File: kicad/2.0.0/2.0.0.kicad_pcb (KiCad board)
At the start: 2 copper layers, 55 parts, among them J1 DIFFX, J2 DIFFY, J3 POWER, J4 SUM, U1 OPA2197, U2 OPA2197, U3 LM317, U4 LM337, U5 OPA2197, U6 OPA197

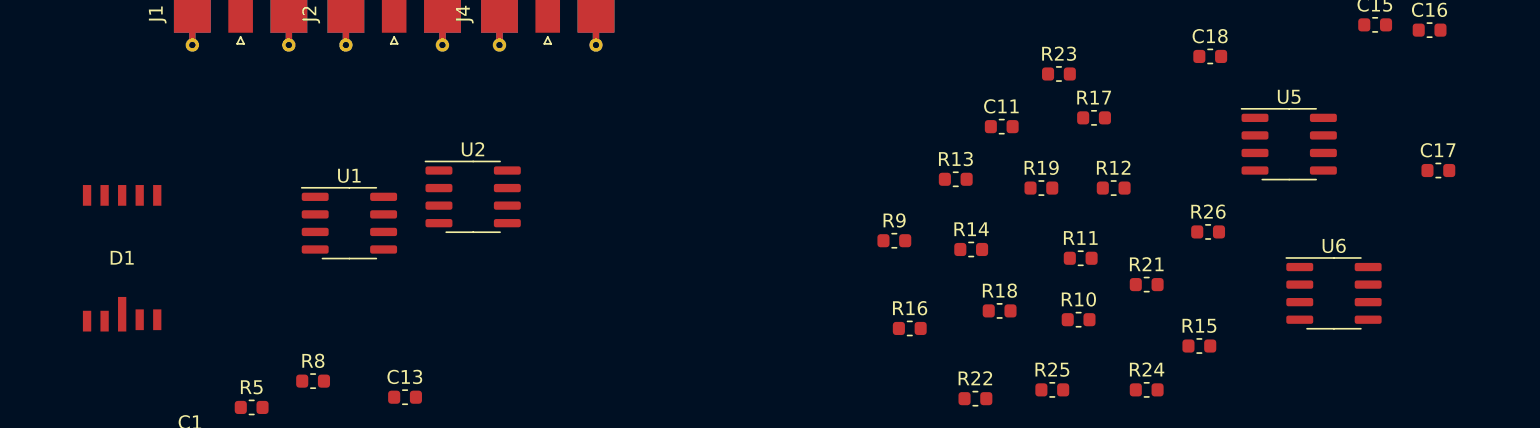
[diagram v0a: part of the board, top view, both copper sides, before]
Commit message: updated footprints of S5990, OPA197 and OPA2197
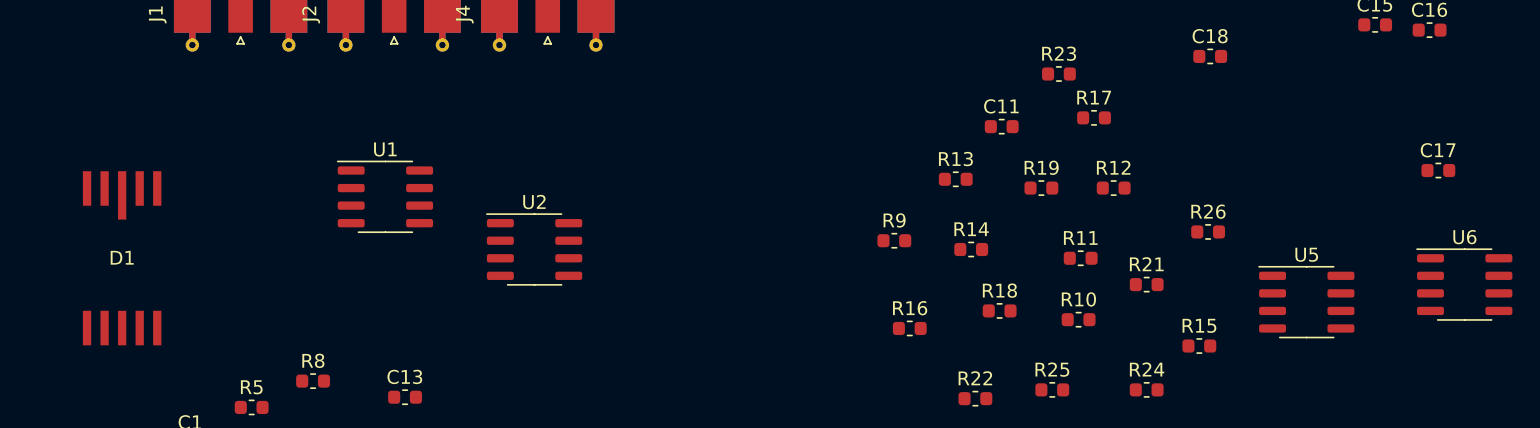
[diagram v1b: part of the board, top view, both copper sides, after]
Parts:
- U1, U2, U5: value OPA2197 -> OPA2197IDR
- U6: value OPA197 -> OPA197IDR
- moved U5 11.5 mm to (137.2, 81.3)
- moved U6 9.48 mm to (148.6, 80.0)
- moved U2 5.85 mm to (81.3, 77.5)
- moved U1 3.23 mm to (70.5, 73.7)
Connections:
- U5 pad 4: +12V -> -12V
- U5 pad 8: -12V -> +12V
- U6 pad 1: /SUM -> (no net)
- U6 pad 6: (no net) -> /SUM
- U6 pad 7: (no net) -> +12V
- U6 pad 8: +12V -> (no net)

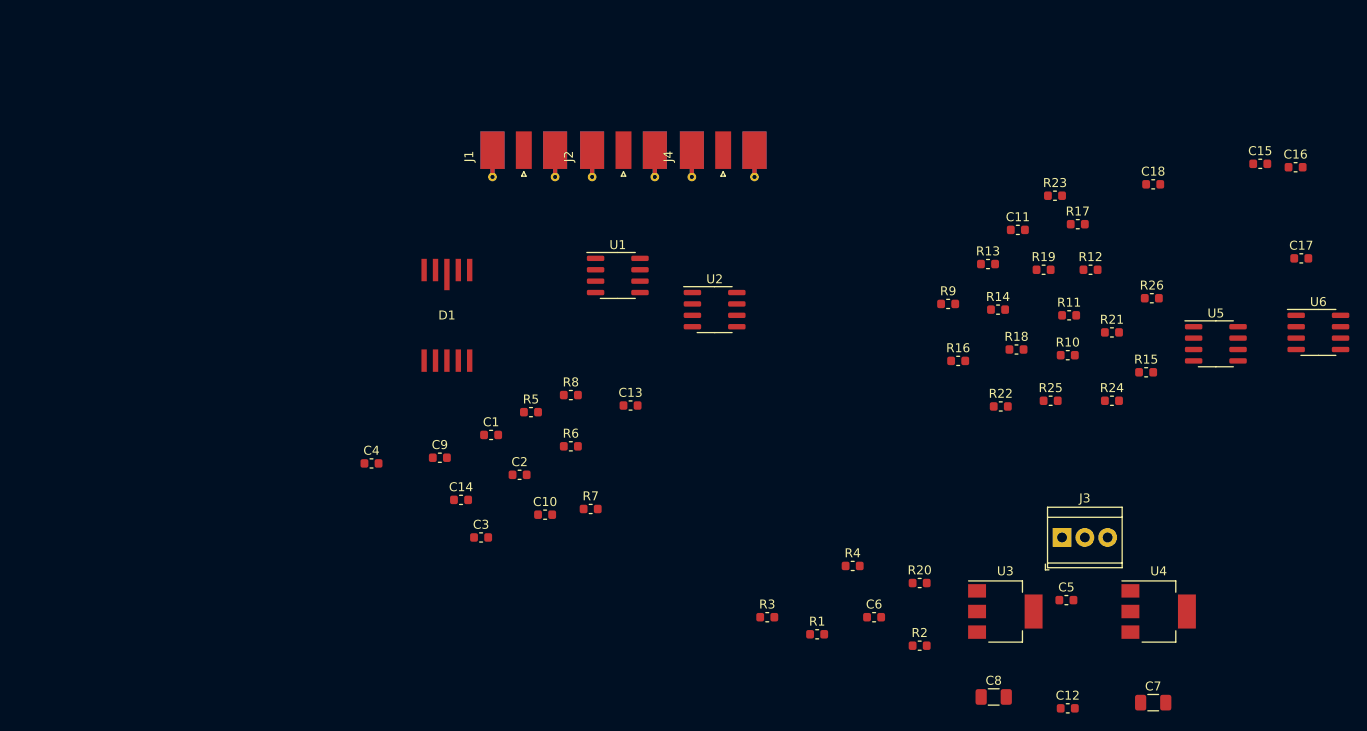
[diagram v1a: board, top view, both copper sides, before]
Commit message: updated S5990 symbol to show pin number
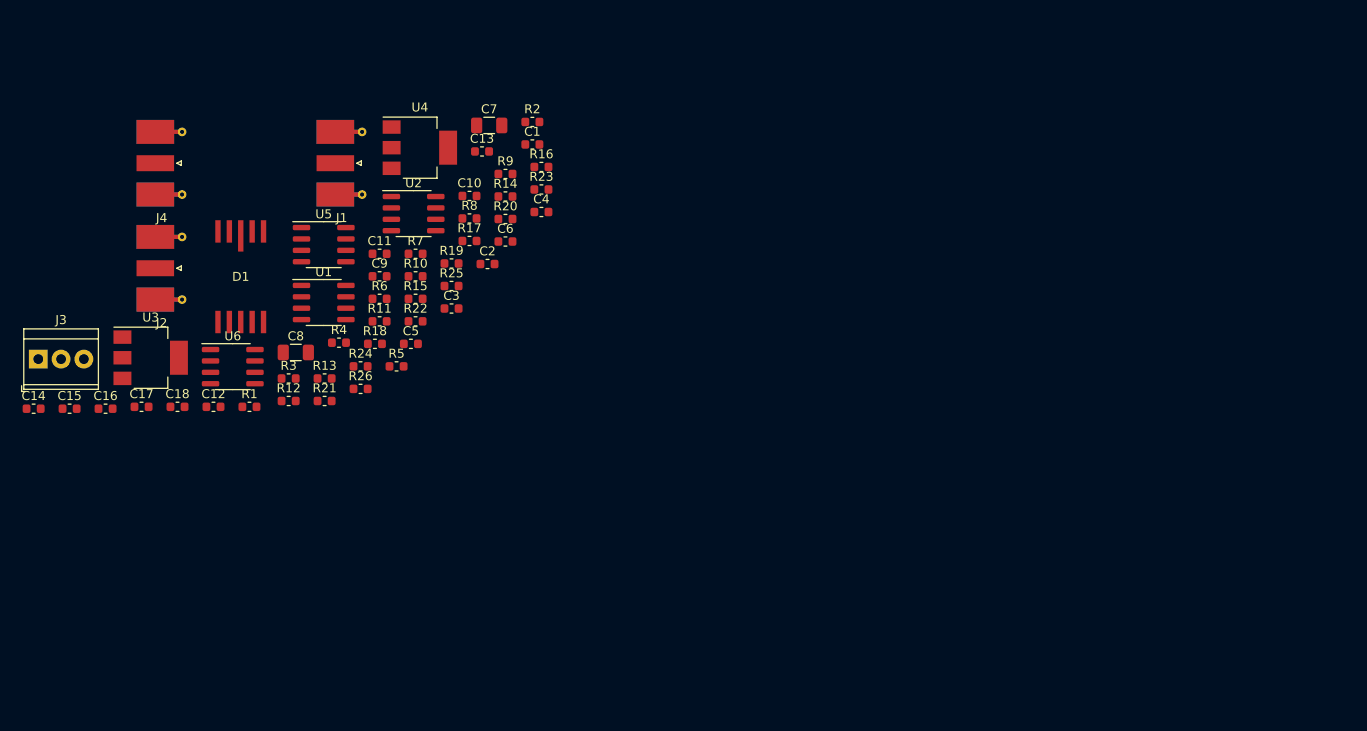
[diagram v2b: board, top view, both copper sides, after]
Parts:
- moved C15 135.5 mm to (9.37, 88.5)
- moved C16 135.4 mm to (13.4, 88.5)
- moved C17 130.3 mm to (17.4, 88.3)
- moved U6 121.1 mm to (27.6, 83.8)
- moved J3 115.9 mm to (5.88, 83.0)
- moved C18 111.6 mm to (21.4, 88.3)
- moved C12 101.0 mm to (25.4, 88.3)
- moved U5 100.1 mm to (37.7, 70.2)
- moved U3 99.4 mm to (18.4, 82.8)
- moved C7 98.1 mm to (56.1, 56.9)
- moved U4 97.3 mm to (48.4, 59.4)
- moved R12 90.6 mm to (33.8, 87.7)
- moved R26 88.8 mm to (41.8, 86.3)
- moved R21 88.1 mm to (37.8, 87.7)
- moved C8 86.8 mm to (34.6, 82.2)
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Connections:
- D1 pad 10: Net-(C10-Pad2) -> Net-(C14-Pad2)
- D1 pad 5: Net-(C14-Pad2) -> Net-(C10-Pad2)
- U6 pad 2: Net-(R21-Pad1) -> Net-(U6-Pad2)
- U6 pad 3: Net-(R25-Pad1) -> Net-(U6-Pad3)
- U6 pad 4: -12V -> Net-(U6-Pad4)
- U6 pad 6: /SUM -> Net-(U6-Pad6)
- U6 pad 7: +12V -> Net-(U6-Pad7)

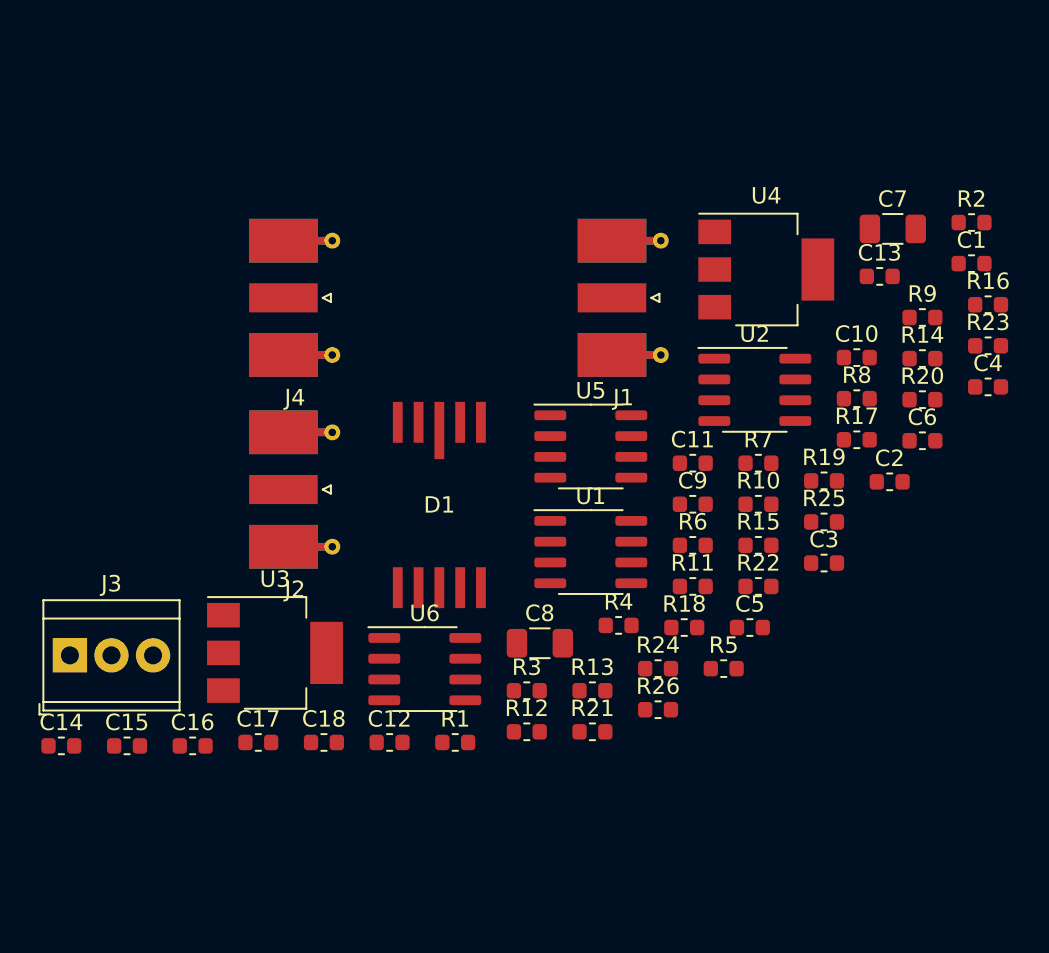
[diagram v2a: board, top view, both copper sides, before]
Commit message: grouped components for 2.0.0 design on pcb
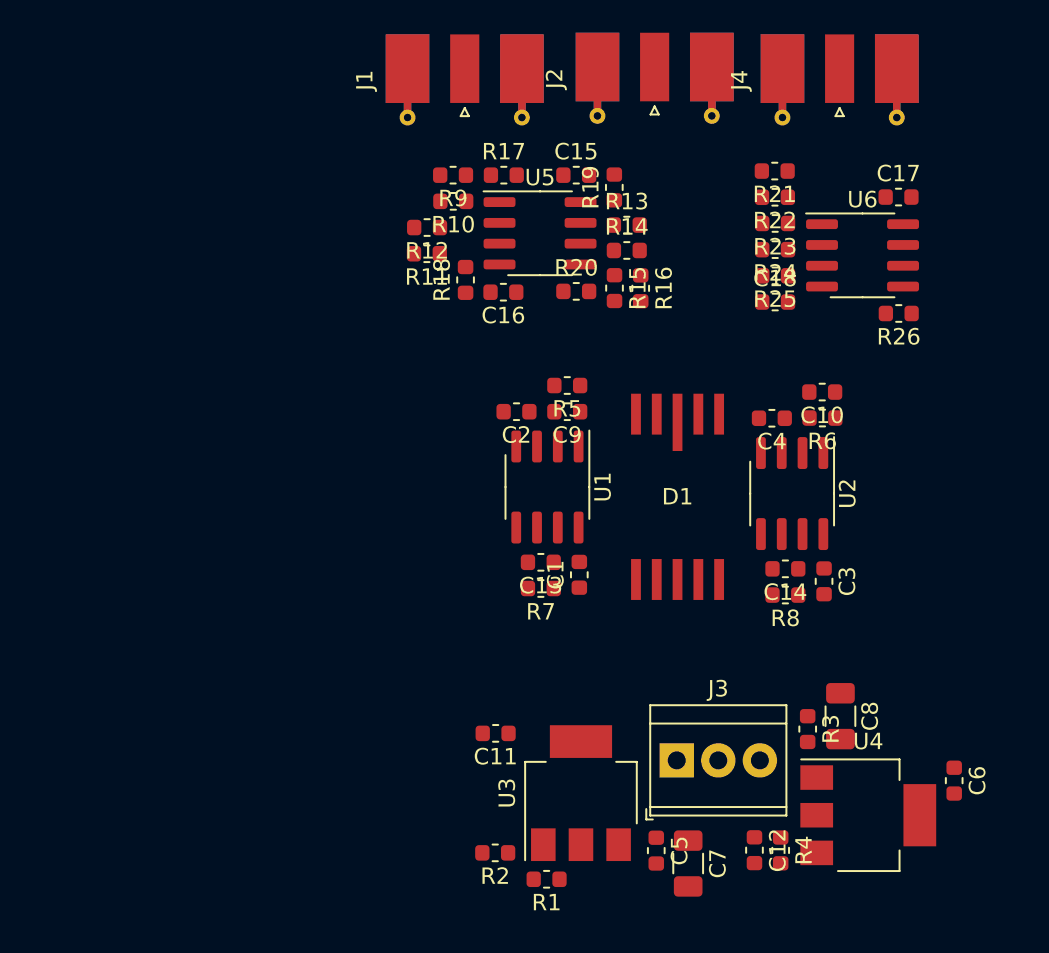
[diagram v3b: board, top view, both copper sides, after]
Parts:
- moved C17 51.4 mm to (56.5, 55.0)
- moved R2 48.3 mm to (31.9, 95.0), turned to 180 degrees
- moved C14 45.5 mm to (49.6, 77.7), turned to 180 degrees
- moved C15 44.4 mm to (36.8, 53.6)
- moved C7 40.7 mm to (43.6, 95.7), turned to 270 degrees
- moved J4 39.5 mm to (52.9, 45.0), turned to 270 degrees
- moved C18 38.5 mm to (49.0, 61.4)
- moved J3 37.6 mm to (43.0, 89.4)
- moved J2 37.3 mm to (41.6, 45.0), turned to 270 degrees
- moved U6 36.8 mm to (54.3, 58.5)
- moved R21 36.0 mm to (48.9, 53.4), turned to 180 degrees
- moved U4 33.9 mm to (54.6, 92.8)
- moved C16 33.6 mm to (32.4, 60.8), turned to 180 degrees
- moved R12 31.4 mm to (27.7, 56.9), turned to 180 degrees
- moved C1 30.6 mm to (37.0, 78.1), turned to 90 degrees
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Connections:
- C13 pad 1: /-X2 -> /-Y2
- C14 pad 1: /-Y2 -> /-X2
- D1 pad 10: Net-(C14-Pad2) -> Net-(C13-Pad2)
- D1 pad 6: Net-(C13-Pad2) -> Net-(C14-Pad2)
- R7 pad 1: /-X2 -> /-Y2
- R8 pad 1: /-Y2 -> /-X2
- U1 pad 7: /-X2 -> /-Y2
- U2 pad 7: /-Y2 -> /-X2
- U6 pad 2: Net-(U6-Pad2) -> Net-(R21-Pad1)
- U6 pad 3: Net-(U6-Pad3) -> Net-(R25-Pad1)
- U6 pad 4: Net-(U6-Pad4) -> -12V
- U6 pad 6: Net-(U6-Pad6) -> /SUM
- U6 pad 7: Net-(U6-Pad7) -> +12V
